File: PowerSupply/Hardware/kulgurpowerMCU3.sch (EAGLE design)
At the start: 135 parts, among them IC2 TPS77333DGK, IC3 REG1117-5, U1 MPU-6000QFN-24, U2 MPU-6000QFN-24, X1 12Mhz, X2 2534-, X3 22-23-2021

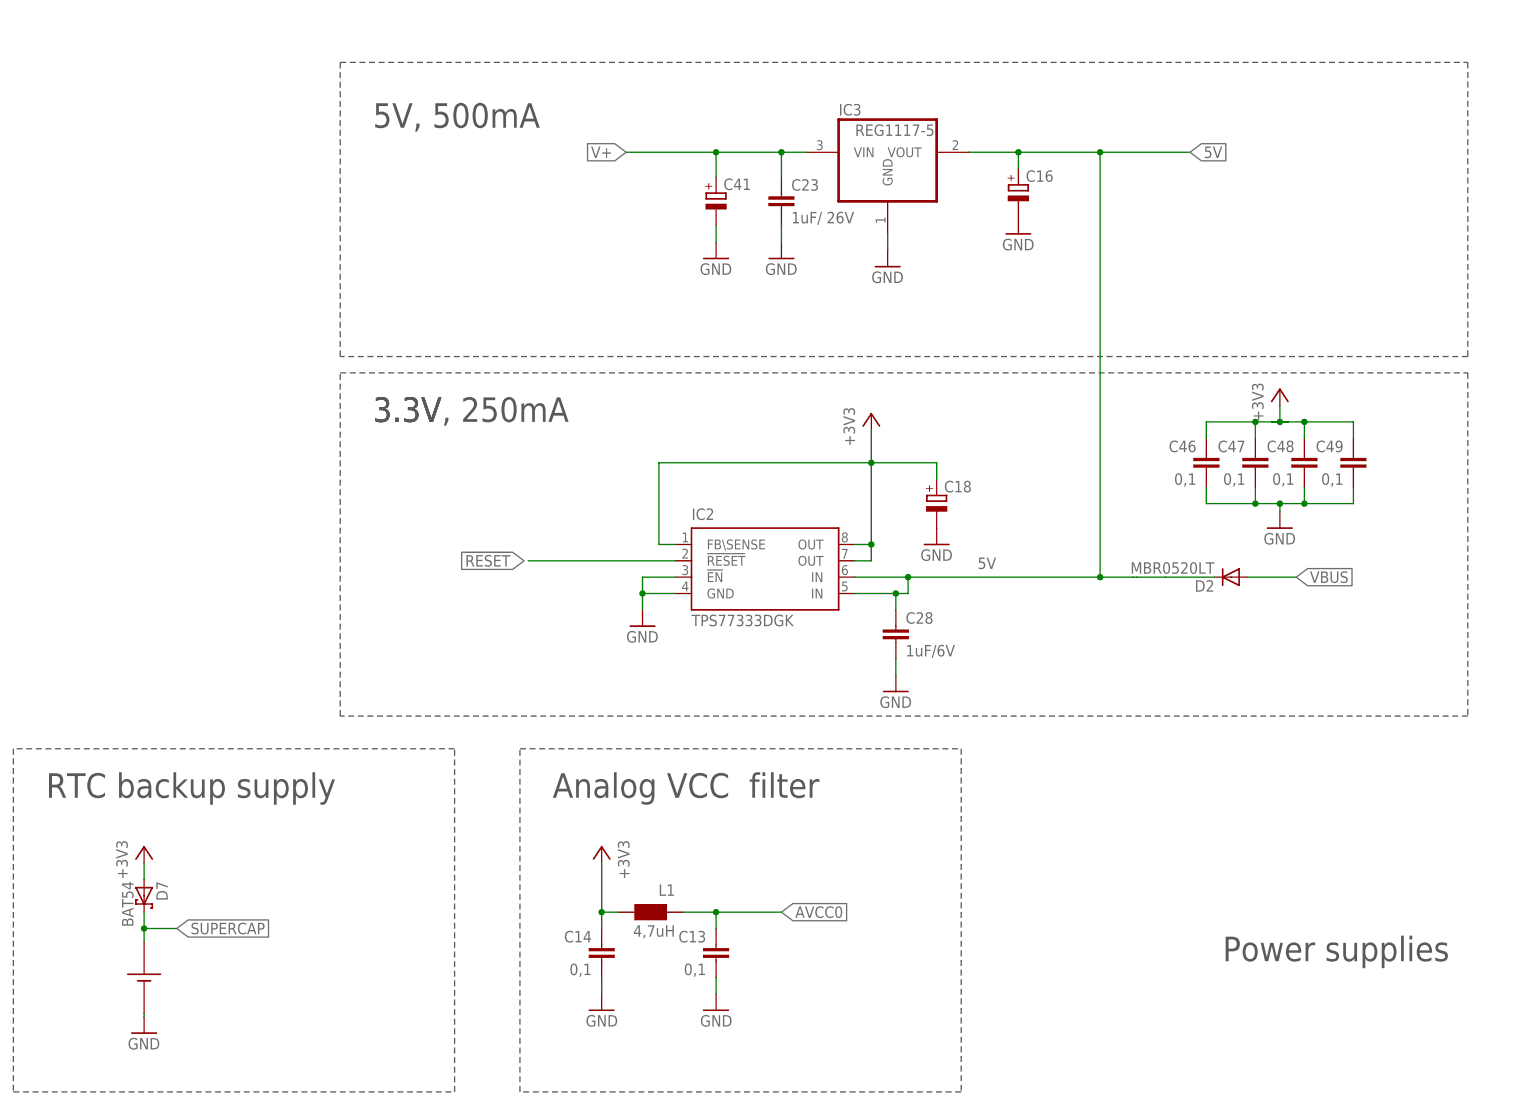
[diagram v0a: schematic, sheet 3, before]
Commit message: Never MCU board of power supply in. 19.2Mhz oscillator added
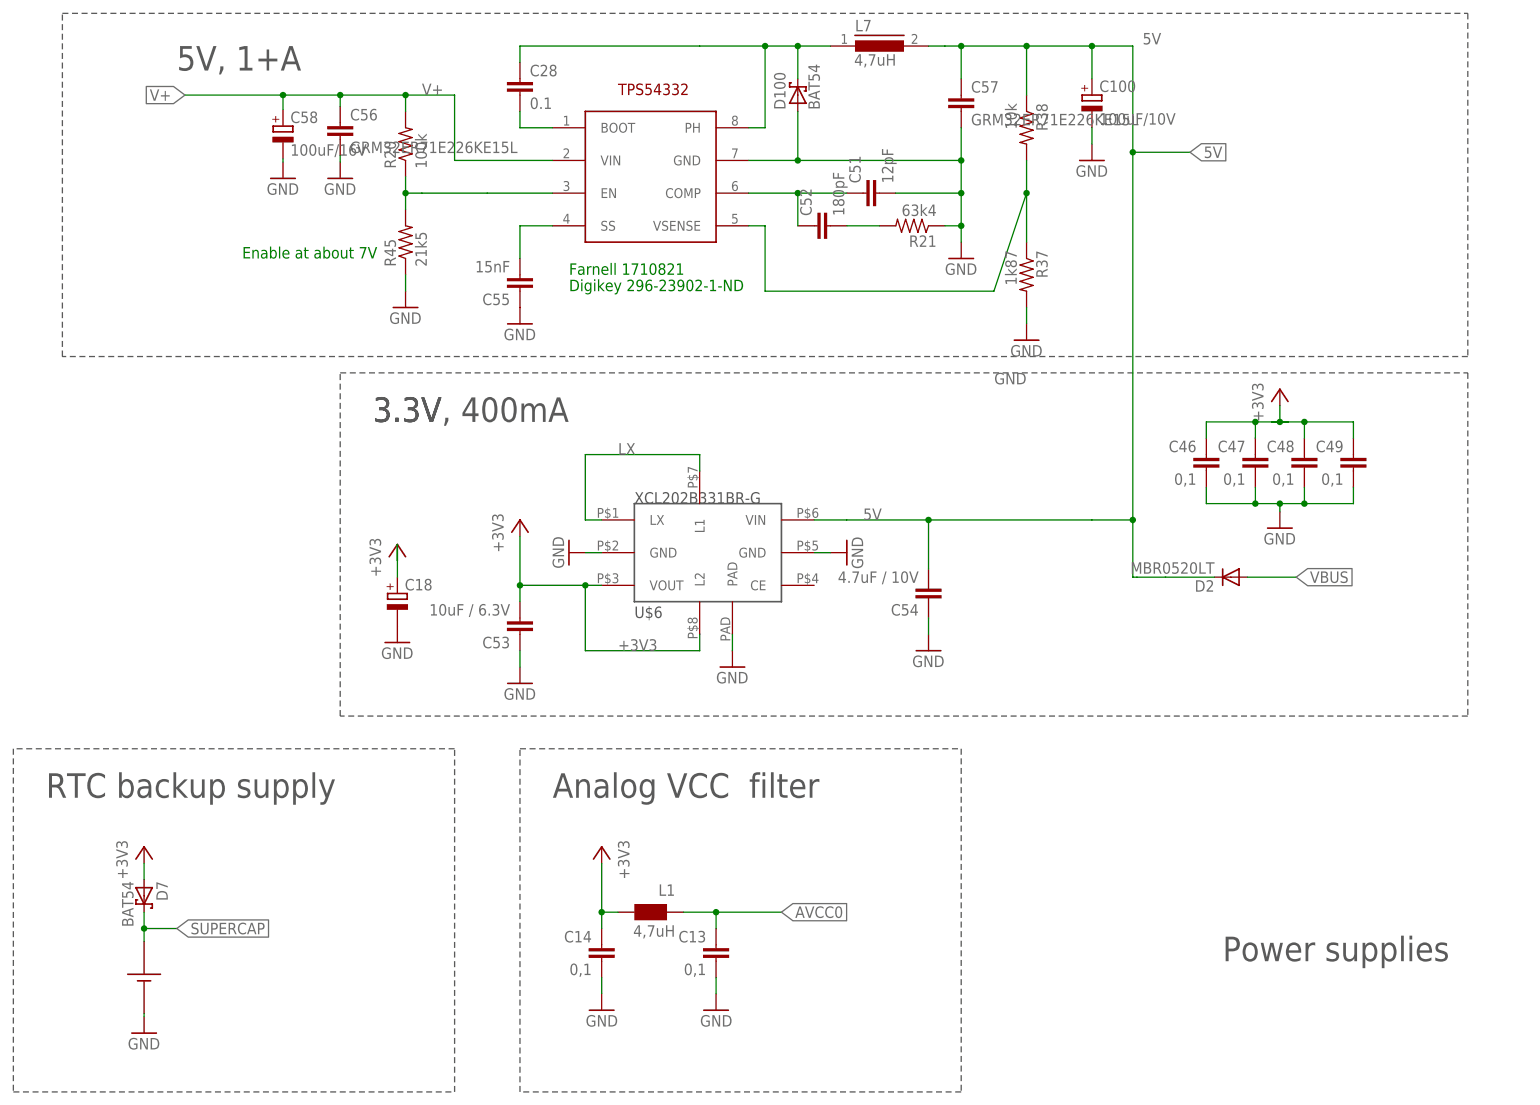
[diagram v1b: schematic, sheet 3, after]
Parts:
- removed C16, C41: (no value), rcl:CPOL-EUC/6032-28R
- removed C23: 1uF/ 26V, resistor:C-EUC0805
- removed IC2: TPS77333DGK, samuel:TPS773
- removed IC3: REG1117-5, burr-brown:REG1117
- added C100: 100uF/10V, rcl:CPOL-EUC/6032-28R
- added C51: 12pF, SparkFun:CAP0603-CAP
- added C52: 180pF, SparkFun:CAP0603-CAP
- added C53: 10uF / 6.3V, rcl:C-EUC0603
- added C54: 4.7uF / 10V, rcl:C-EUC0603
- added C55: 15nF, SparkFun:CAP0603-CAP
- added C56, C57: GRM32ER71E226KE15L, rcl:C-EUC1210
- added C58: 100uF/16V, rcl:CPOL-EUC/6032-28R
- added D100: BAT54, diode:BAT54
- added L7: 4,7uH, inductors:DR73
- added R20: 100k, SparkFun:RESISTOR0603-RES
- added R21: 63k4, SparkFun:RESISTOR0603-RES
- added R37: 1k87, SparkFun:RESISTOR0603-RES
- added R38: 10k, SparkFun:RESISTOR0603-RES
- added R45: 21k5, SparkFun:RESISTOR0603-RES
- added TP1: TPB1,27, testpad:TPB1,27
- added U$4: ASE, crystal:ASE
- added U$5: TPS54332, tonu:TPS54332
- added U$6: XCL202B331BR-G, XCL202:XCL202
- C28: value 1uF/6V -> 0.1; device resistor:C-EUC0603 -> SparkFun:CAP0603-CAP
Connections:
- new net ENABLE_PANDA: R20.1, R45.2, U$5.EN
- new net LX: U$6.L1, U$6.LX
- new net N$109: C51.1, C52.1, U$5.COMP
- new net N$120: C52.2, R21.2
- new net N$121: C28.2, U$5.BOOT
- new net N$125: R37.1, R38.2, U$5.VSENSE
- new net N$138: C28.1, D100.C, L7.1, U$5.PH
- new net N$26: U$4.OUT, U1.FSYNC, U2.FSYNC
- new net N$5: U1.CLKIN
- new net N$7: U2.CLKIN
- new net N$96: C55.2, U$5.SS
- net !RESET: no longer IC2.!RESET
- net +3V3: now also C53.2, TP1.TP, U$4.TRI, U$4.VDD, U$6.L2, U$6.VOUT; no longer IC2.FB\SENSE, IC2.OUT@1, IC2.OUT@2
- net 5V: now also C100.+, C54.2, C57.1, L7.2, R38.1, U$6.VIN; no longer C16.+, C28.1, IC2.IN@1, IC2.IN@2, IC3.VOUT
- net GND: now also C100.-, C51.2, C53.1, C54.1, C55.1, C56.2, C57.2, C58.-, D100.A, R21.1, R37.2, R45.1, U$4.GND, U$5.GND, U$6.GND@2, U$6.GND@5, U$6.PAD; no longer C16.-, C23.2, C28.2, C41.-, IC2.!EN, IC2.GND, IC3.GND, U1.CLKIN, U2.CLKIN
- net V+: now also C56.1, C58.+, R20.2, U$5.VIN; no longer C23.1, C41.+, IC3.VIN
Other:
- note added: "3.3V, 400mA"
- note added: "5V, 1+A"
- note added: "Digikey 296-23902-1-ND"
- note added: "Enable at about 7V"
- note added: "Farnell 1710821"
- note removed: "3.3V, 250mA"
- note removed: "5V, 500mA"
- moved on the sheet: C18, C19, C20, C21, C24, C25, C26, C28, U1, U2
